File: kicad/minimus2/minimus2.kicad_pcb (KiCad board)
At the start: 2 copper layers, 55 x 55.5 mm, 74 parts, among them J1 PROG_SER, J2 LM, J3 LM, Q1 SSM6N58NU_LF, Q2 SSM6N58NU_LF, Q3 DMN3051L, SW1 RESET, SW2 USER_A, SW4 SW_SPDT, U1 LSM6DSRTR, U2 STM32U575CITx, U3 DRV8835, U4 AS5047D, U5 AS5047D, U6 AP2210N-5.0TRG1, U7 AP2210N-3.3TRG1

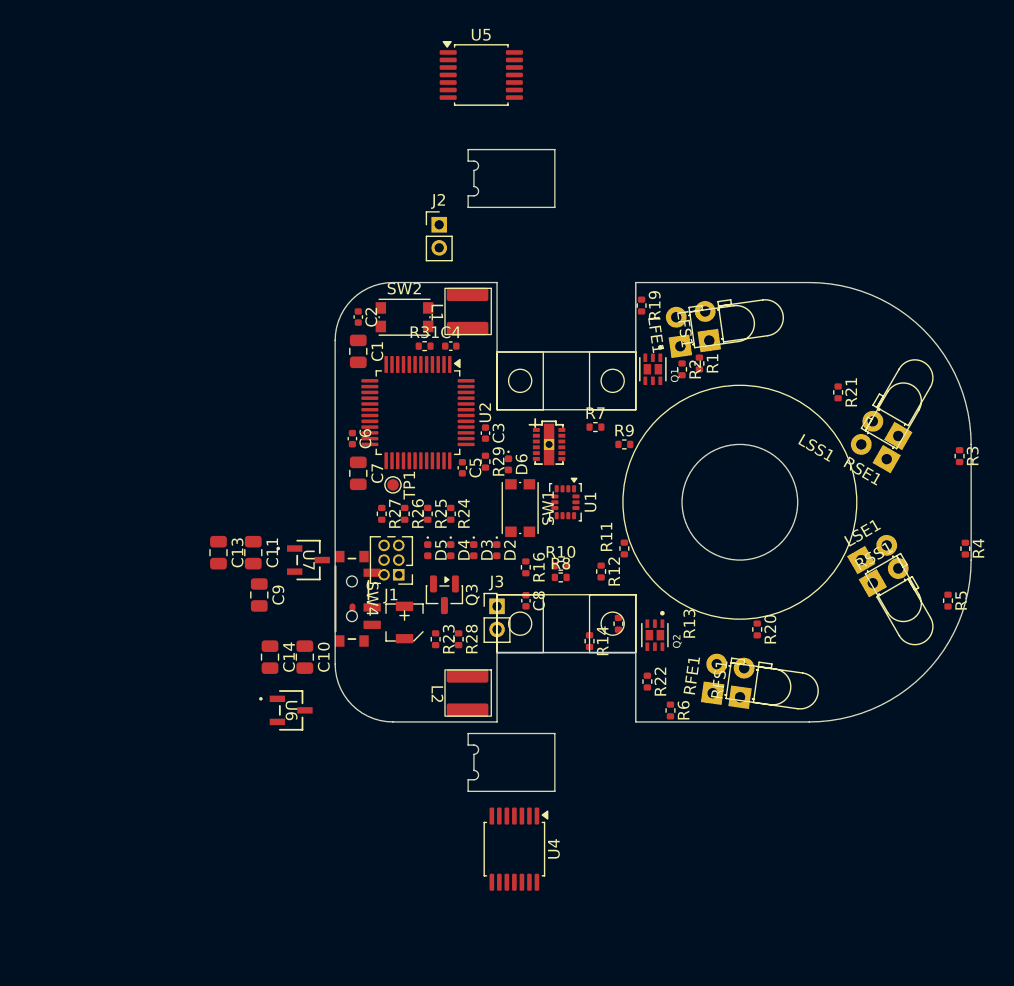
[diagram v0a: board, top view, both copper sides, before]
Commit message: update PCB with motors
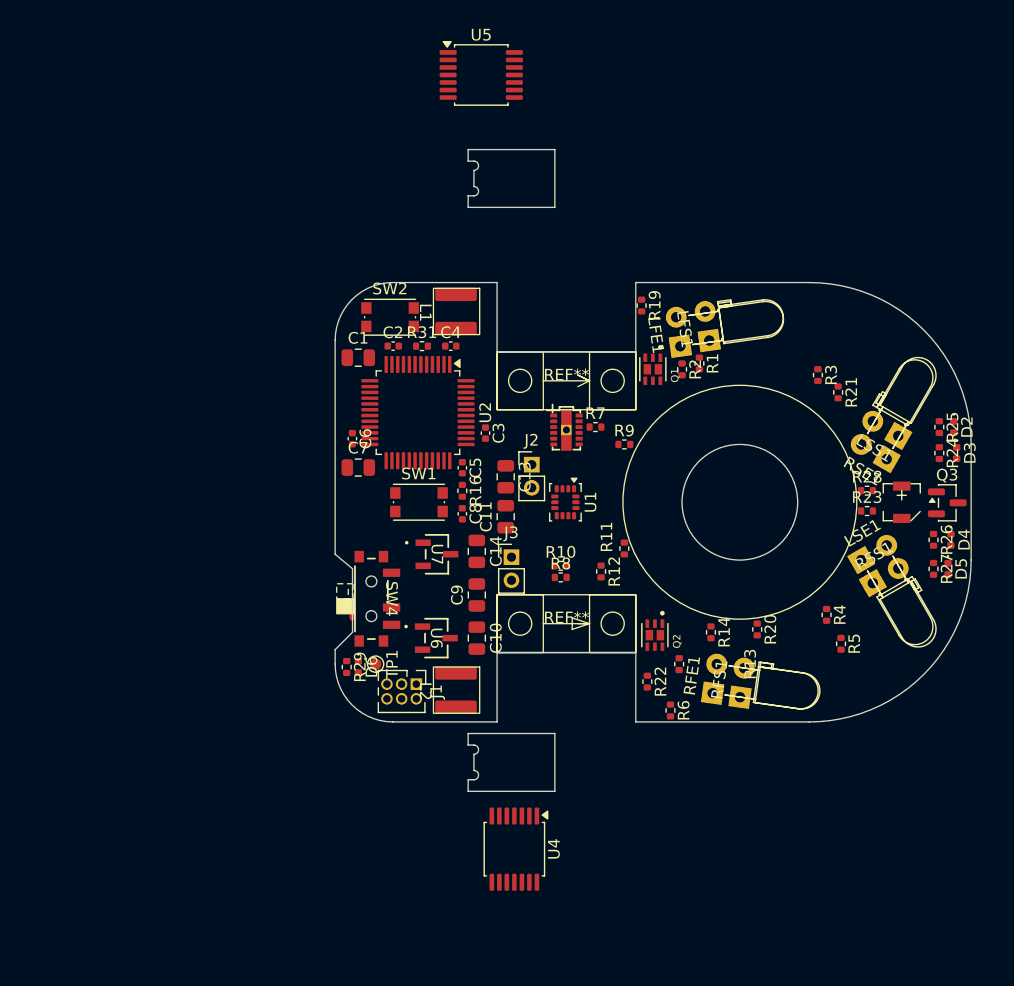
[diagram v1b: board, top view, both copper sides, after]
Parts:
- added REF**: motor_mount_left, minimus:motor_mount_left, F.Cu at (100.0, 89.5)
- added REF**: motor_mount_right, minimus:motor_mount_right, F.Cu at (100.0, 110.5)
- LFE1, LSE1, RFE1, RSE1: footprint LED_THT:LED_D3.0mm_Horizontal_O1.27mm_Z2.0mm_IRBlack -> minimus:LED_D3.0mm_Horizontal_O3.81mm_Z6.0mm
- moved R27 48.0 mm to (131.8, 105.8)
- moved R26 45.8 mm to (131.8, 103.2)
- moved D5 45.0 mm to (133.0, 105.8)
- moved R25 44.9 mm to (132.2, 93.5)
- moved LS1 44.2 mm to (129.0, 100.0)
- moved Q3 44.2 mm to (132.9, 100.0), turned to 0 degrees
- moved D4 43.3 mm to (133.2, 103.2)
- moved D3 42.6 mm to (133.8, 95.8)
- moved R24 42.6 mm to (132.2, 95.8)
- moved D2 40.9 mm to (133.5, 93.5)
- moved R23 38.9 mm to (126.0, 100.8), turned to 0 degrees
- moved R28 37.6 mm to (126.0, 99.0), turned to 0 degrees
- moved C13 25.7 mm to (94.8, 97.8)
- moved J2 22.2 mm to (97.0, 96.8)
- moved C11 22.1 mm to (94.8, 101.2), turned to 90 degrees
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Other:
- outline, holes or cut-outs redrawn

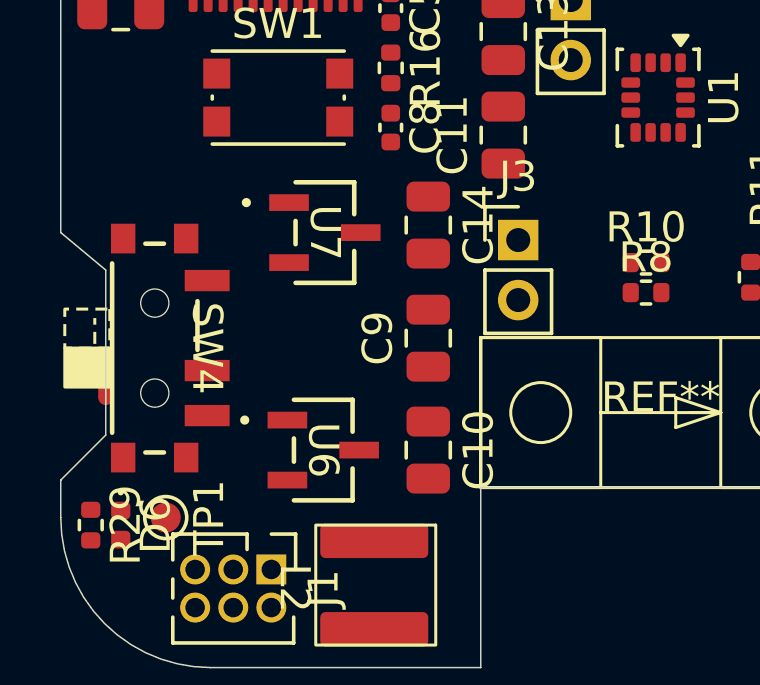
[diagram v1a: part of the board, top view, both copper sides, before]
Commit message: update power supply
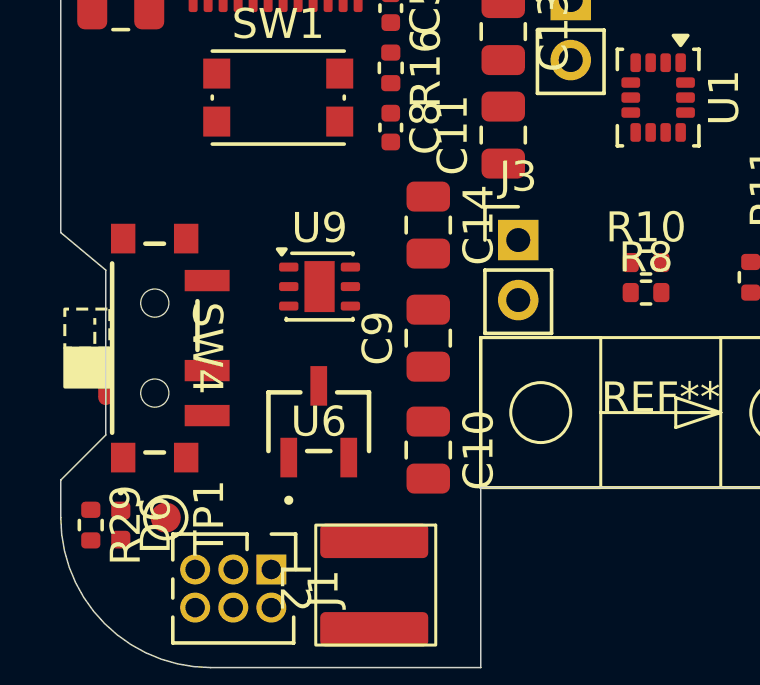
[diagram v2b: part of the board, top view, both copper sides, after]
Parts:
- removed U7: AP2210N-3.3TRG1, minimus:AP2210N-x.xTRG1_DIO
- added U9: AP7370-50FDC, minimus:DFN-6-1EP_2x2mm_P0.65mm_EP1.01x1.7mm, F.Cu at (88.6, 106.3)
- U6: value AP2210N-5.0TRG1 -> AP2210N-3.3TRG1
- moved U6 0.96 mm to (88.6, 110.8), turned to 0 degrees
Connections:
- C10 pad 1: +5V -> +BATT
- C14 pad 1: +3.3V -> +5V

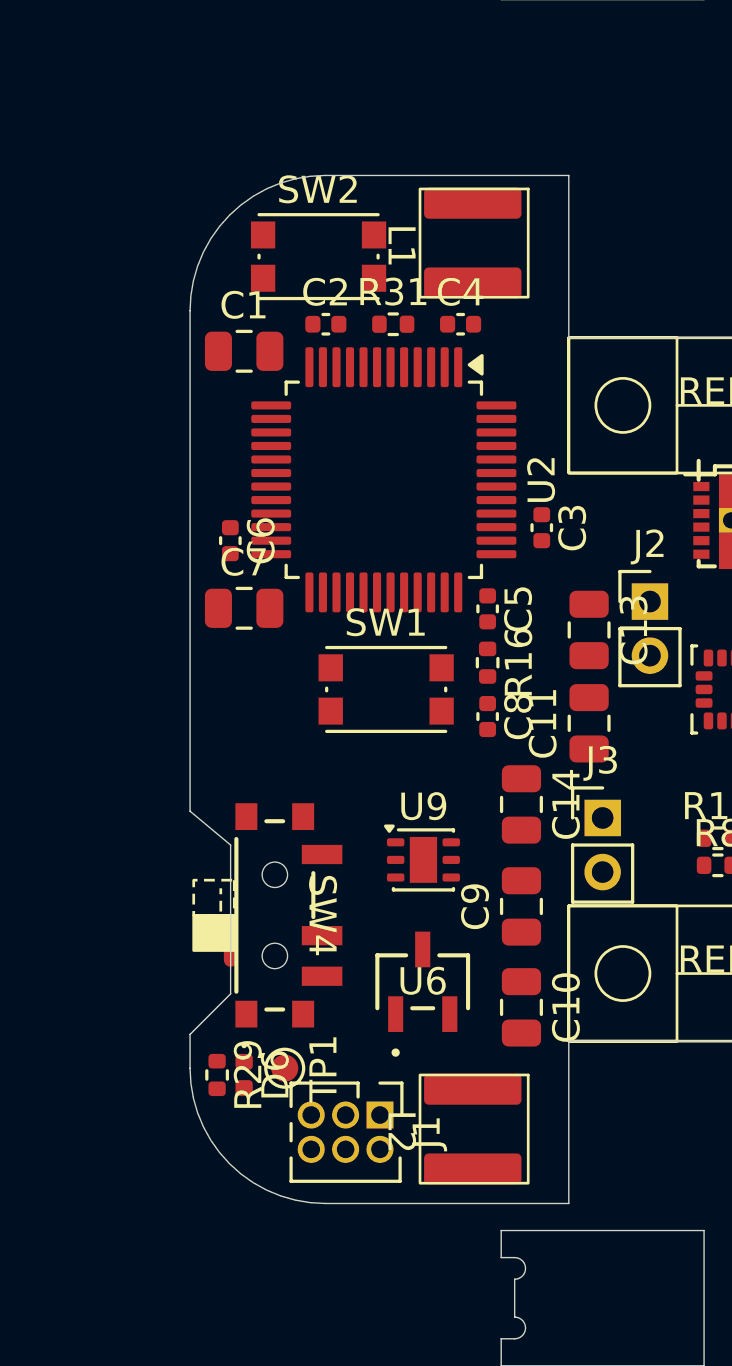
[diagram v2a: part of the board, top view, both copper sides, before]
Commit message: extend the mouse by 5mm to rear
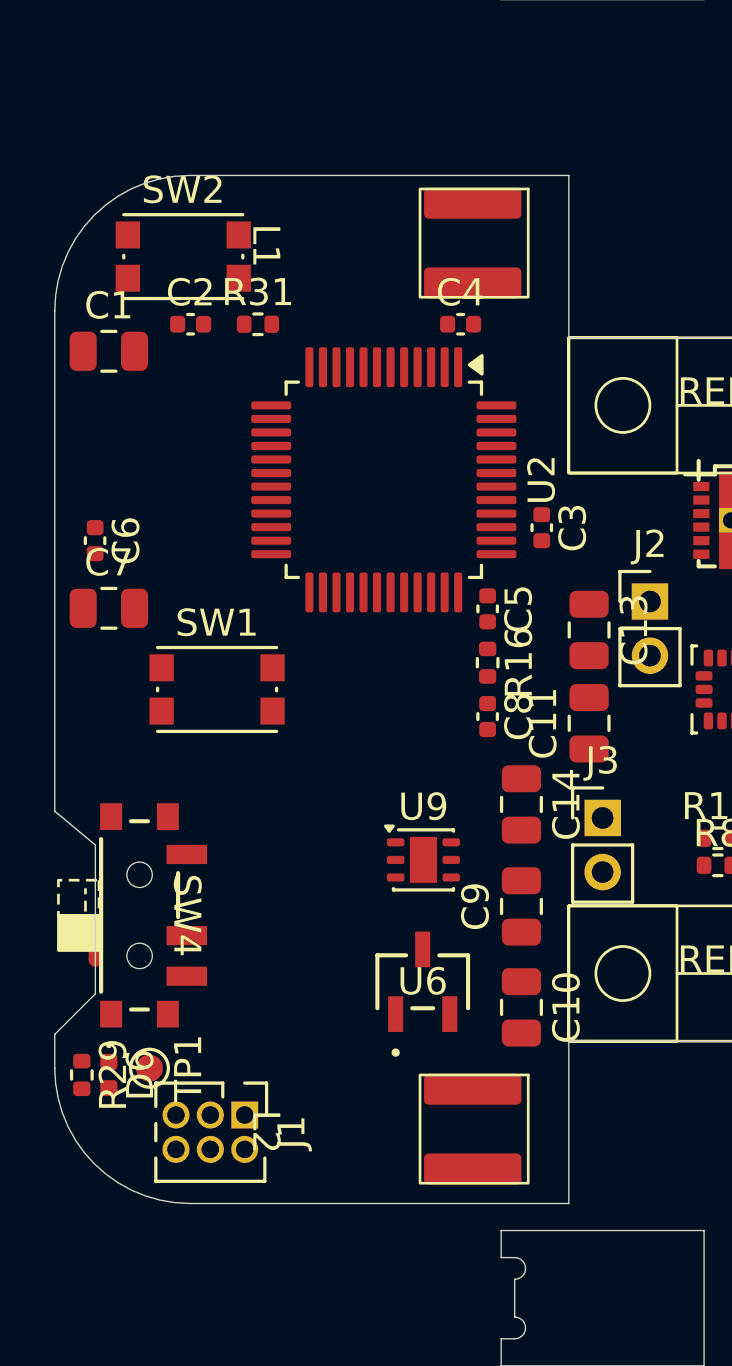
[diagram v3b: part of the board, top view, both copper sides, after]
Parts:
- moved SW1 6.25 mm to (81.0, 100.0)
- moved C1 5.00 mm to (77.0, 87.5)
- moved C2 5.00 mm to (80.0, 86.5)
- moved C6 5.00 mm to (76.5, 94.5)
- moved C7 5.00 mm to (77.0, 97.0)
- moved D6 5.00 mm to (77.0, 114.2)
- moved J1 5.00 mm to (82.0, 115.7)
- moved NT1 5.00 mm to (76.5, 109.5)
- moved R29 5.00 mm to (76.0, 114.2)
- moved R31 5.00 mm to (82.5, 86.5)
- moved SW2 5.00 mm to (79.8, 84.0)
- moved SW4 5.00 mm to (78.1, 108.4)
- moved TP1 5.00 mm to (78.5, 114.0)
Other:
- board size 55 x 55.5 mm -> 60 x 55.5 mm
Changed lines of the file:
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@@
 	(footprint "Connector_PinHeader_1.27mm:PinHeader_2x03_P1.27mm_Vertical"
 		(layer "F.Cu")
-		(at 87.02 115.73 -90)
+		(at 82.02 115.73 -90)
 		(descr "Through hole straight pin header, 2x03, 1.27mm pitch, double rows")
 		(tags "Through hole pin header THT 2x03 1.27mm double row")
@@
 	(footprint "Button_Switch_SMD:SW_Push_1P1T_NO_CK_KMR2"
 		(layer "F.Cu")
-		(at 84.75 84)
+		(at 79.75 84)
 		(descr "CK components KMR2 tactile switch http://www.ckswitches.com/media/1479/kmr2.pdf")
 		(tags "tactile switch kmr2")
@@
 	(footprint "Resistor_SMD:R_0402_1005Metric"
 		(layer "F.Cu")
-		(at 87.51 86.5)
+		(at 82.51 86.5)
 		(descr "Resistor SMD 0402 (1005 Metric), square (rectangular) end terminal, IPC-7351 nominal, (Body size source: IPC-SM-782 page 72, https://www.pcb-3d.com/wordpress/wp-content/uploads/ipc-sm-782a_amendment_1_and_2.pdf), generated with kicad-footprint-generator")
 		(tags "resistor")
@@
 		(fp_line
 			(start 0 0)
-			(end 0.000001 3.81)
+			(end 0.000002 3.81)
 			(stroke
 				(width 0.1)
@@
 		)
 		(fp_line
-			(start 0.000001 3.81)
+			(start 0.000002 3.81)
 			(end 0 0)
 			(stroke
@@
 		(descr "4mmx4mm Inductor")
 		(property "Reference" "L1"
-			(at 0.1 2.7 270)
+			(at 0.1 7.7 270)
 			(unlocked yes)
 			(layer "F.SilkS")
@@
 	(footprint "Capacitor_SMD:C_0805_2012Metric"
 		(layer "F.Cu")
-		(at 82 97)
+		(at 77 97)
 		(descr "Capacitor SMD 0805 (2012 Metric), square (rectangular) end terminal, IPC-7351 nominal, (Body size source: IPC-SM-782 page 76, https://www.pcb-3d.com/wordpress/wp-content/uploads/ipc-sm-782a_amendment_1_and_2.pdf, https://docs.google.com/spreadsheets/d/1BsfQQcO9C6DZCsRaXUlFlo91Tg2WpOkGARC1WS5S8t0/edit?usp=sharing), generated with kicad-footprint-generator")
 		(tags "capacitor")
@@
 	(footprint "minimus:CUS-12TB_NDC"
 		(layer "F.Cu")
-		(at 83.135121 108.35002 -90)
+		(at 78.135121 108.35002 -90)
 		(tags "CUS-12TB ")
 		(property "Reference" "SW4"
@@
 	(footprint "NetTie:NetTie-2_SMD_Pad0.5mm"
 		(layer "F.Cu")
-		(at 81.5 109.5 -90)
+		(at 76.5 109.5 -90)
 		(descr "Net tie, 2 pin, 0.5mm square SMD pads")
 		(tags "net tie")
@@
 	(footprint "Capacitor_SMD:C_0805_2012Metric"
 		(layer "F.Cu")
-		(at 82 87.5)
+		(at 77 87.5)
 		(descr "Capacitor SMD 0805 (2012 Metric), square (rectangular) end terminal, IPC-7351 nominal, (Body size source: IPC-SM-782 page 76, https://www.pcb-3d.com/wordpress/wp-content/uploads/ipc-sm-782a_amendment_1_and_2.pdf, https://docs.google.com/spreadsheets/d/1BsfQQcO9C6DZCsRaXUlFlo91Tg2WpOkGARC1WS5S8t0/edit?usp=sharing), generated with kicad-footprint-generator")
 		(tags "capacitor")
@@
 	(footprint "TestPoint:TestPoint_Pad_D1.0mm"
 		(layer "F.Cu")
-		(at 83.5 114 -90)
+		(at 78.5 114 -90)
 		(descr "SMD pad as test Point, diameter 1.0mm")
 		(tags "test point SMD pad")
@@
 		)
 		(fp_text user "${REFERENCE}"
-			(at 1.27 3.120002 98)
+			(at 1.27 3.120003 98)
 			(layer "F.Fab")
 			(effects
@@
 	(footprint "LED_SMD:LED_0402_1005Metric"
 		(layer "F.Cu")
-		(at 82 114.25 -90)
+		(at 77 114.25 -90)
 		(descr "LED SMD 0402 (1005 Metric), square (rectangular) end terminal, IPC-7351 nominal, (Body size source: http://www.tortai-tech.com/upload/download/2011102023233369053.pdf), generated with kicad-footprint-generator")
 		(tags "LED")
@@
 		(fp_line
 			(start 0 0)
-			(end -0.000001 3.81)
+			(end -0.000002 3.81)
 			(stroke
 				(width 0.1)
@@
 		)
 		(fp_line
-			(start -0.000001 3.81)
+			(start -0.000002 3.81)
 			(end 0 0)
 			(stroke
@@
 	(footprint "Button_Switch_SMD:SW_Push_1P1T_NO_CK_KMR2"
 		(layer "F.Cu")
-		(at 87.25 100)
+		(at 81 100)
 		(descr "CK components KMR2 tactile switch http://www.ckswitches.com/media/1479/kmr2.pdf")
 		(tags "tactile switch kmr2")
@@
 	(footprint "Capacitor_SMD:C_0402_1005Metric"
 		(layer "F.Cu")
-		(at 85.02 86.5)
+		(at 80.02 86.5)
 		(descr "Capacitor SMD 0402 (1005 Metric), square (rectangular) end terminal, IPC-7351 nominal, (Body size source: IPC-SM-782 page 76, https://www.pcb-3d.com/wordpress/wp-content/uploads/ipc-sm-782a_amendment_1_and_2.pdf), generated with kicad-footprint-generator")
 		(tags "capacitor")
@@
 		(descr "4mmx4mm Inductor")
 		(property "Reference" "L2"
-			(at 0.1 2.7 270)
+			(at 0.1 7.7 270)
 			(unlocked yes)
 			(layer "F.SilkS")
@@
 	(footprint "Capacitor_SMD:C_0402_1005Metric"
 		(layer "F.Cu")
-		(at 81.49 94.5 -90)
+		(at 76.49 94.5 -90)
 		(descr "Capacitor SMD 0402 (1005 Metric), square (rectangular) end terminal, IPC-7351 nominal, (Body size source: IPC-SM-782 page 76, https://www.pcb-3d.com/wordpress/wp-content/uploads/ipc-sm-782a_amendment_1_and_2.pdf), generated with kicad-footprint-generator")
 		(tags "capacitor")
@@
 	(footprint "Resistor_SMD:R_0402_1005Metric"
 		(layer "F.Cu")
-		(at 81 114.25 -90)
+		(at 76 114.25 -90)
 		(descr "Resistor SMD 0402 (1005 Metric), square (rectangular) end terminal, IPC-7351 nominal, (Body size source: IPC-SM-782 page 72, https://www.pcb-3d.com/wordpress/wp-content/uploads/ipc-sm-782a_amendment_1_and_2.pdf), generated with kicad-footprint-generator")
 		(tags "resistor")
@@
 	)
 	(gr_line
-		(start 81.5 111.25)
-		(end 80 112.75)
+		(start 76.5 111.25)
+		(end 75 112.75)
 		(stroke
 			(width 0.05)
@@
 	)
 	(gr_line
-		(start 85 119)
+		(start 80 119)
 		(end 94 119)
 		(stroke
@@
 	)
 	(gr_line
-		(start 80 112.75)
-		(end 80 114)
+		(start 75 112.75)
+		(end 75 114)
 		(stroke
 			(width 0.05)
@@
 	)
 	(gr_line
-		(start 81.5 105.75)
-		(end 81.5 111.25)
+		(start 76.5 105.75)
+		(end 76.5 111.25)
 		(stroke
 			(width 0.05)
@@
 	)
 	(gr_line
-		(start 80 104.5)
-		(end 81.5 105.75)
+		(start 75 104.5)
+		(end 76.5 105.75)
 		(stroke
 			(width 0.05)
@@
 	)
 	(gr_arc
-		(start 85 119)
-		(mid 81.464466 117.535534)
-		(end 80 114)
+		(start 80 119)
+		(mid 76.464466 117.535534)
+		(end 75 114)
 		(stroke
 			(width 0.05)
@@
 	(gr_line
 		(start 94 81)
-		(end 85 81)
+		(end 80 81)
 		(stroke
 			(width 0.05)
@@
 	)
 	(gr_arc
-		(start 80 86)
-		(mid 81.464466 82.464466)
-		(end 85 81)
+		(start 75 86)
+		(mid 76.464466 82.464466)
+		(end 80 81)
 		(stroke
 			(width 0.05)
@@
 	)
 	(gr_line
-		(start 80 86)
-		(end 80 104.5)
+		(start 75 86)
+		(end 75 104.5)
 		(stroke
 			(width 0.05)

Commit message: update EDA
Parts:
- added C12: 100nF, Capacitor_SMD:C_0402_1005Metric, F.Cu at (62.1, 126.0)
- added C15: 100nF, Capacitor_SMD:C_0402_1005Metric, F.Cu at (90.1, 128.1)
- added R15: 47k, Resistor_SMD:R_0402_1005Metric, F.Cu at (65.5, 124.5)
- added R17: 47k, Resistor_SMD:R_0402_1005Metric, F.Cu at (90.8, 131.0)
- added R18: 47k, Resistor_SMD:R_0402_1005Metric, F.Cu at (90.8, 133.0)
- added R30: 47k, Resistor_SMD:R_0402_1005Metric, F.Cu at (90.8, 135.0)
- added R32: 47k, Resistor_SMD:R_0402_1005Metric, F.Cu at (62.1, 129.2)
- added R33: 47k, Resistor_SMD:R_0402_1005Metric, F.Cu at (62.5, 131.7)
- moved U5 68.5 mm to (97.3, 131.4)
- moved R29 31.3 mm to (91.7, 87.2)
- moved D6 31.1 mm to (92.6, 87.3)
- moved U4 27.4 mm to (68.1, 129.5)
- moved J2 17.9 mm to (86.5, 82.3)
- moved J3 15.3 mm to (86.5, 117.3), turned to 180 degrees
- moved C11 9.82 mm to (85.7, 105.0)
- moved R7 7.91 mm to (109.7, 90.2)
- moved R11 7.59 mm to (109.8, 109.9)
- moved U3 7.12 mm to (96.6, 100.0)
- moved R9 4.89 mm to (107.5, 90.8)
- moved R12 4.71 mm to (106.7, 108.9)
- moved C13 1.45 mm to (93.7, 96.8)
- turned L1 to 90 degrees
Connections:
- U4 pad 1: unconnected-(U4-~{CS}-Pad1) -> Net-(U4-~{CS})
- U4 pad 11: unconnected-(U4-VDD-Pad11) -> +3.3V
- U4 pad 12: unconnected-(U4-VDD3V3-Pad12) -> +3.3V
- U4 pad 2: unconnected-(U4-CLK-Pad2) -> Net-(U4-CLK)
- U4 pad 4: unconnected-(U4-MOSI-Pad4) -> Net-(U4-MOSI)
- U4 pad 5: unconnected-(U4-TST-Pad5) -> GND
- U4 pad 6: unconnected-(U4-B-Pad6) -> LENC_B
- U4 pad 7: unconnected-(U4-A-Pad7) -> LENC_A
- U5 pad 1: unconnected-(U5-~{CS}-Pad1) -> Net-(U5-~{CS})
- U5 pad 11: unconnected-(U5-VDD-Pad11) -> +3.3V
- U5 pad 12: unconnected-(U5-VDD3V3-Pad12) -> +3.3V
- U5 pad 2: unconnected-(U5-CLK-Pad2) -> Net-(U5-CLK)
- U5 pad 4: unconnected-(U5-MOSI-Pad4) -> Net-(U5-MOSI)
- U5 pad 5: unconnected-(U5-TST-Pad5) -> GND
- U5 pad 6: unconnected-(U5-B-Pad6) -> RENC_B
- U5 pad 7: unconnected-(U5-A-Pad7) -> RENC_A
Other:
- board size 60 x 55.5 mm -> 67.7 x 58.8 mm
